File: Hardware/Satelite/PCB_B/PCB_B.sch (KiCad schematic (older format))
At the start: 11 parts, among them IC1 MCP1642B-50I_MS, J1 Conector_PCB_B-C, J2 Conector_PCB_A-B, U1 MIC5323-3.3YD5_TR

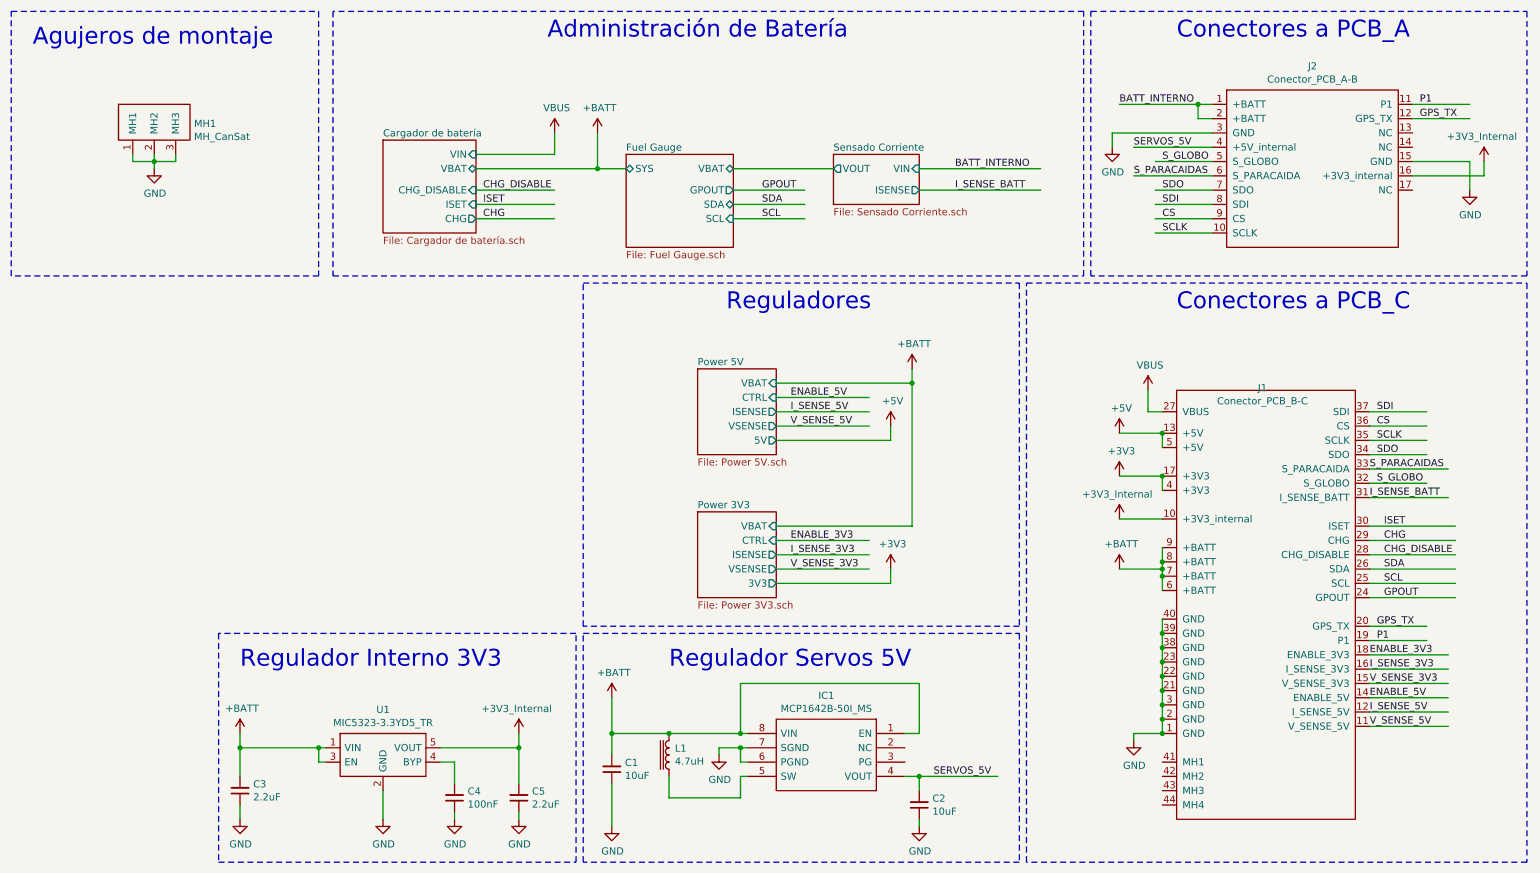
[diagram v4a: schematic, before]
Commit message: Numeros de parte para PCB_B
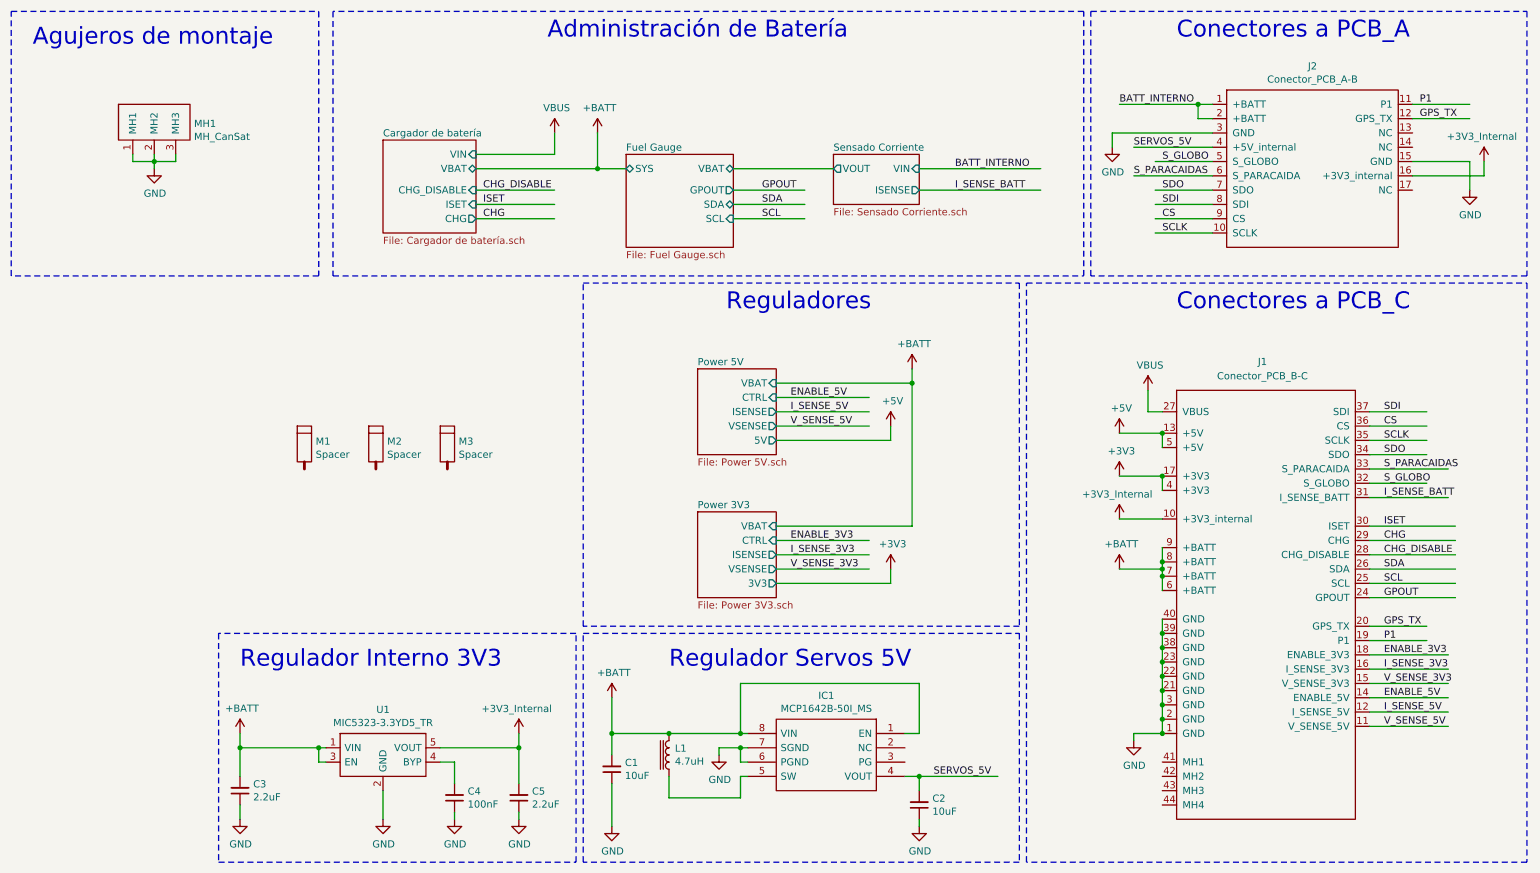
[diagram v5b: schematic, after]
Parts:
- added M1, M2, M3: Spacer, AXTEC:Empty_Footprint, symbol AXTEC_IC:Spacer
- IC1: Manufacturer Part Number (none) -> MCP1642B-50I/MS; Manufacturer_Part_Number MCP1642B-50I/MS -> (none)
- J1: Manufacturer Part Number (none) -> 10132798-022100LF; Quantity (none) -> 2
- J2: Manufacturer Part Number 1 (none) -> CES-103-01-T-S; Manufacturer Part Number 2 (none) -> CES-104-01-T-S; Quantity 1 (none) -> 4; Quantity 2 (none) -> 2
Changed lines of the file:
@@
 Wire Wire Line
 	10450 3350 10050 3350
-Text Label 10100 3650 0    50   ~ 0
+Text Label 10150 3650 0    50   ~ 0
 SDO
-Text Label 10100 3350 0    50   ~ 0
+Text Label 10150 3350 0    50   ~ 0
 SDI
-Text Label 10100 3450 0    50   ~ 0
+Text Label 10150 3450 0    50   ~ 0
 CS
-Text Label 10100 3550 0    50   ~ 0
+Text Label 10150 3550 0    50   ~ 0
 SCLK
-Text Label 10100 3850 0    50   ~ 0
+Text Label 10150 3850 0    50   ~ 0
 S_GLOBO
-Text Label 10050 3750 0    50   ~ 0
+Text Label 10150 3750 0    50   ~ 0
 S_PARACAIDAS
 Wire Wire Line
@@
 Wire Wire Line
 	10450 4850 10050 4850
-Text Label 10100 4850 0    50   ~ 0
+Text Label 10150 4850 0    50   ~ 0
 GPS_TX
-Text Label 10100 4950 0    50   ~ 0
+Text Label 10150 4950 0    50   ~ 0
 P1
 Wire Notes Line
@@
 F 2 "AXTEC:Conector_PCB_A-B" H 9250 1950 50  0001 C CNN
 F 3 "" H 9250 1950 50  0001 C CNN
+F 4 "CES-103-01-T-S" H 9500 1500 50  0001 C CNN "Manufacturer Part Number 1"
+F 5 "4" H 9500 1500 50  0001 C CNN "Quantity 1"
+F 6 "CES-104-01-T-S" H 9500 1500 50  0001 C CNN "Manufacturer Part Number 2"
+F 7 "2" H 9500 1500 50  0001 C CNN "Quantity 2"
 	1    9500 1500
 	1    0    0    -1
@@
 Wire Wire Line
 	10050 5550 10600 5550
-Text Label 10050 5450 0    50   ~ 0
+Text Label 10150 5450 0    50   ~ 0
 I_SENSE_5V
-Text Label 10050 5550 0    50   ~ 0
+Text Label 10150 5550 0    50   ~ 0
 V_SENSE_5V
 Wire Wire Line
@@
 Wire Wire Line
 	10050 5250 10600 5250
-Text Label 10050 5150 0    50   ~ 0
+Text Label 10150 5150 0    50   ~ 0
 I_SENSE_3V3
-Text Label 10050 5250 0    50   ~ 0
+Text Label 10150 5250 0    50   ~ 0
 V_SENSE_3V3
 Wire Wire Line
 	10050 3950 10600 3950
-Text Label 10050 3950 0    50   ~ 0
+Text Label 10150 3950 0    50   ~ 0
 I_SENSE_BATT
 Text Label 10150 4650 0    50   ~ 0
@@
 F 5 "1.1" H 7750 5400 50  0001 L CNN "Height"
 F 6 "Microchip" H 7750 5300 50  0001 L CNN "Manufacturer_Name"
-F 7 "MCP1642B-50I/MS" H 7750 5200 50  0001 L CNN "Manufacturer_Part_Number"
-F 8 "" H 7750 5100 50  0001 L CNN "RS Part Number"
-F 9 "" H 7750 5000 50  0001 L CNN "RS Price/Stock"
-F 10 "70567327" H 7750 4900 50  0001 L CNN "Allied_Number"
-F 11 "https://www.alliedelec.com/microchip-technology-inc-mcp1642b-50i-ms/70567327/" H 7750 4800 50  0001 L CNN "Allied Price/Stock"
-F 12 "MCP1642B-50I/MS" H 7750 4700 50  0001 L CNN "Arrow Part Number"
-F 13 "https://www.arrow.com/en/products/mcp1642b-50ims/microchip-technology" H 7750 4600 50  0001 L CNN "Arrow Price/Stock"
+F 7 "MCP1642B-50I/MS" H 7750 5200 50  0001 L CNN "Manufacturer Part Number"
+F 8 "70567327" H 7750 4900 50  0001 L CNN "Allied_Number"
+F 9 "https://www.alliedelec.com/microchip-technology-inc-mcp1642b-50i-ms/70567327/" H 7750 4800 50  0001 L CNN "Allied Price/Stock"
+F 10 "MCP1642B-50I/MS" H 7750 4700 50  0001 L CNN "Arrow Part Number"
+F 11 "https://www.arrow.com/en/products/mcp1642b-50ims/microchip-technology" H 7750 4600 50  0001 L CNN "Arrow Price/Stock"
 	1    6800 5600
 	-1   0    0    -1
@@
 U 1 1 5BD2AA01
 P 9300 3900
-F 0 "J1" H 9300 4617 50  0000 C CNN
-F 1 "Conector_PCB_B-C" H 9300 4525 50  0000 C CNN
+F 0 "J1" H 9300 4800 50  0000 C CNN
+F 1 "Conector_PCB_B-C" H 9300 4700 50  0000 C CNN
 F 2 "AXTEC:Conector_PCB_B-C_Lado_B" H 9200 4650 50  0001 C CNN
 F 3 "" H 9200 4650 50  0001 C CNN
+F 4 "10132798-022100LF" H 9300 3900 50  0001 C CNN "Manufacturer Part Number"
+F 5 "2" H 9300 3900 50  0001 C CNN "Quantity"
 	1    9300 3900
 	1    0    0    -1
@@
 Wire Wire Line
 	10600 5350 10050 5350
-Text Label 10050 5050 0    50   ~ 0
+Text Label 10150 5050 0    50   ~ 0
 ENABLE_3V3
-Text Label 10050 5350 0    50   ~ 0
+Text Label 10150 5350 0    50   ~ 0
 ENABLE_5V
 Wire Wire Line
@@
 Wire Wire Line
 	8500 3350 8500 3200
+$Comp
+L AXTEC_IC:Spacer M1
+U 1 1 5C28AC86
+P 2600 3550
+F 0 "M1" H 2679 3543 50  0000 L CNN
+F 1 "Spacer" H 2679 3451 50  0000 L CNN
+F 2 "AXTEC:Empty_Footprint" H 2500 3700 50  0001 C CNN
+F 3 "https://www.mouser.com/datasheet/2/181/R30-301-1135805.pdf" H 2600 3800 50  0001 C CNN
+F 4 "R30-3011002" H 2679 3405 50  0001 L CNN "Manufacturer Part Number"
+	1    2600 3550
+	1    0    0    -1
+$EndComp
+$Comp
+L AXTEC_IC:Spacer M2
+U 1 1 5C28AE04
+P 3100 3550
+F 0 "M2" H 3179 3543 50  0000 L CNN
+F 1 "Spacer" H 3179 3451 50  0000 L CNN
+F 2 "AXTEC:Empty_Footprint" H 3000 3700 50  0001 C CNN
+F 3 "https://www.mouser.com/datasheet/2/181/R30-301-1135805.pdf" H 3100 3800 50  0001 C CNN
+F 4 "R30-3011002" H 3179 3405 50  0001 L CNN "Manufacturer Part Number"
+	1    3100 3550
+	1    0    0    -1
+$EndComp
+$Comp
+L AXTEC_IC:Spacer M3
+U 1 1 5C28AE40
+P 3600 3550
+F 0 "M3" H 3679 3543 50  0000 L CNN
+F 1 "Spacer" H 3679 3451 50  0000 L CNN
+F 2 "AXTEC:Empty_Footprint" H 3500 3700 50  0001 C CNN
+F 3 "https://www.mouser.com/datasheet/2/181/R30-301-1135805.pdf" H 3600 3800 50  0001 C CNN
+F 4 "R30-3011002" H 3679 3405 50  0001 L CNN "Manufacturer Part Number"
+	1    3600 3550
+	1    0    0    -1
+$EndComp
 $EndSCHEMATC

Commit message: Separadores de 12mm entre A y B para dar lugar a la bateria
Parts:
- M1, M2, M3: Manufacturer Part Number R30-3011002 -> R30-3011202
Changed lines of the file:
@@
 F 2 "AXTEC:Empty_Footprint" H 2500 3700 50  0001 C CNN
 F 3 "https://www.mouser.com/datasheet/2/181/R30-301-1135805.pdf" H 2600 3800 50  0001 C CNN
-F 4 "R30-3011002" H 2679 3405 50  0001 L CNN "Manufacturer Part Number"
+F 4 "R30-3011202" H 2679 3405 50  0001 L CNN "Manufacturer Part Number"
 	1    2600 3550
 	1    0    0    -1
@@
 F 2 "AXTEC:Empty_Footprint" H 3000 3700 50  0001 C CNN
 F 3 "https://www.mouser.com/datasheet/2/181/R30-301-1135805.pdf" H 3100 3800 50  0001 C CNN
-F 4 "R30-3011002" H 3179 3405 50  0001 L CNN "Manufacturer Part Number"
+F 4 "R30-3011202" H 3179 3405 50  0001 L CNN "Manufacturer Part Number"
 	1    3100 3550
 	1    0    0    -1
@@
 F 2 "AXTEC:Empty_Footprint" H 3500 3700 50  0001 C CNN
 F 3 "https://www.mouser.com/datasheet/2/181/R30-301-1135805.pdf" H 3600 3800 50  0001 C CNN
-F 4 "R30-3011002" H 3679 3405 50  0001 L CNN "Manufacturer Part Number"
+F 4 "R30-3011202" H 3679 3405 50  0001 L CNN "Manufacturer Part Number"
 	1    3600 3550
 	1    0    0    -1

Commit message: Eliminados pines no usados del conector A-B
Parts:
- J2: Quantity 1 4 -> 3
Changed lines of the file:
@@
 F 3 "" H 9250 1950 50  0001 C CNN
 F 4 "CES-103-01-T-S" H 9500 1500 50  0001 C CNN "Manufacturer Part Number 1"
-F 5 "4" H 9500 1500 50  0001 C CNN "Quantity 1"
+F 5 "3" H 9500 1500 50  0001 C CNN "Quantity 1"
 F 6 "CES-104-01-T-S" H 9500 1500 50  0001 C CNN "Manufacturer Part Number 2"
 F 7 "2" H 9500 1500 50  0001 C CNN "Quantity 2"

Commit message: BOM PCB_B y corrección a numeros de parte
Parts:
- J2: Manufacturer Part Number (none) -> CES-103-01-T-S; Manufacturer Part Number 1 CES-103-01-T-S -> (none); Quantity (none) -> 3; Quantity 1 3 -> (none)
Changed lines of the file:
@@
 F 2 "AXTEC:Conector_PCB_A-B" H 9250 1950 50  0001 C CNN
 F 3 "" H 9250 1950 50  0001 C CNN
-F 4 "CES-103-01-T-S" H 9500 1500 50  0001 C CNN "Manufacturer Part Number 1"
-F 5 "3" H 9500 1500 50  0001 C CNN "Quantity 1"
+F 4 "CES-103-01-T-S" H 9500 1500 50  0001 C CNN "Manufacturer Part Number"
+F 5 "3" H 9500 1500 50  0001 C CNN "Quantity"
 F 6 "CES-104-01-T-S" H 9500 1500 50  0001 C CNN "Manufacturer Part Number 2"
 F 7 "2" H 9500 1500 50  0001 C CNN "Quantity 2"
